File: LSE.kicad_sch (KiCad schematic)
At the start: 4 parts, among them Y2 32.758kHz

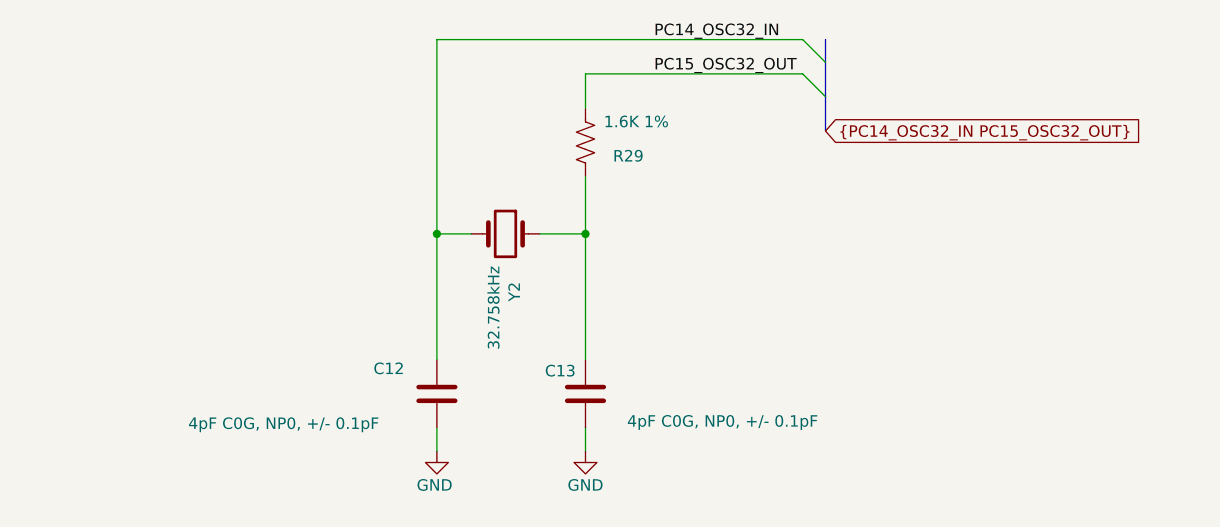
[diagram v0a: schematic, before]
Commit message: layout with F411 roughly good but needs work.
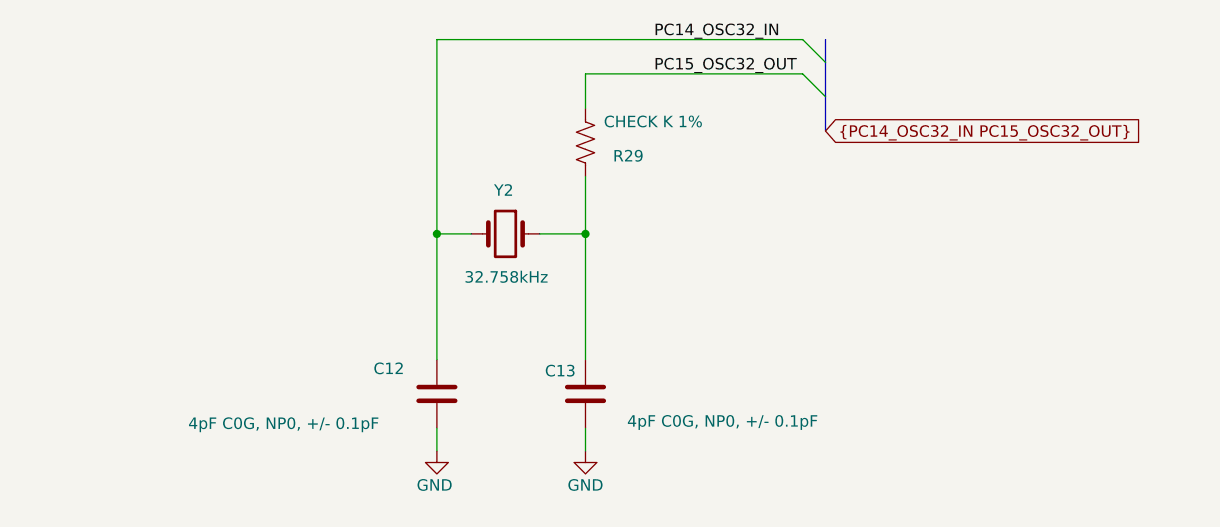
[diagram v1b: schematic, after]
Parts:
- C12, C13: footprint ProjectLib:C_0201_0603Metric -> ProjectLib:C_0603_1608Metric
- R29: value 1.6K 1% -> CHECK K 1%; footprint (none) -> ProjectLib:R_0603_1608Metric
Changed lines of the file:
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@@
 			)
 		)
-		(property "Footprint" "ProjectLib:C_0201_0603Metric"
+		(property "Footprint" "ProjectLib:C_0603_1608Metric"
 			(at 128.5748 109.22 0)
 			(effects
@@
 			)
 		)
-		(property "Footprint" "ProjectLib:C_0201_0603Metric"
+		(property "Footprint" "ProjectLib:C_0603_1608Metric"
 			(at 112.0648 109.22 0)
 			(effects
@@
 			)
 		)
-		(property "Value" "1.6K 1%"
+		(property "Value" "CHECK K 1%"
 			(at 131.572 82.804 0)
 			(effects
@@
 			)
 		)
-		(property "Footprint" ""
+		(property "Footprint" "ProjectLib:R_0603_1608Metric"
 			(at 130.556 85.344 90)
 			(effects
@@
 		(dnp no)
 		(property "Reference" "Y2"
-			(at 121.666 100.584 90)
+			(at 119.38 90.424 0)
 			(effects
 				(font
@@
 		)
 		(property "Value" "32.758kHz"
-			(at 119.38 98.806 90)
+			(at 116.078 100.076 0)
 			(effects
 				(font
@@
 			)
 		)
-		(property "Datasheet" "https://www.microcrystal.com/fileadmin/Media/Products/32kHz/Datasheet/CM9V-T1A.pdf"
+		(property "Datasheet" "~"
 			(at 120.65 95.25 0)
 			(effects

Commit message: Moats complete. No errors. Net tie needs better zone and check crystals, BoM, etc. And general review.
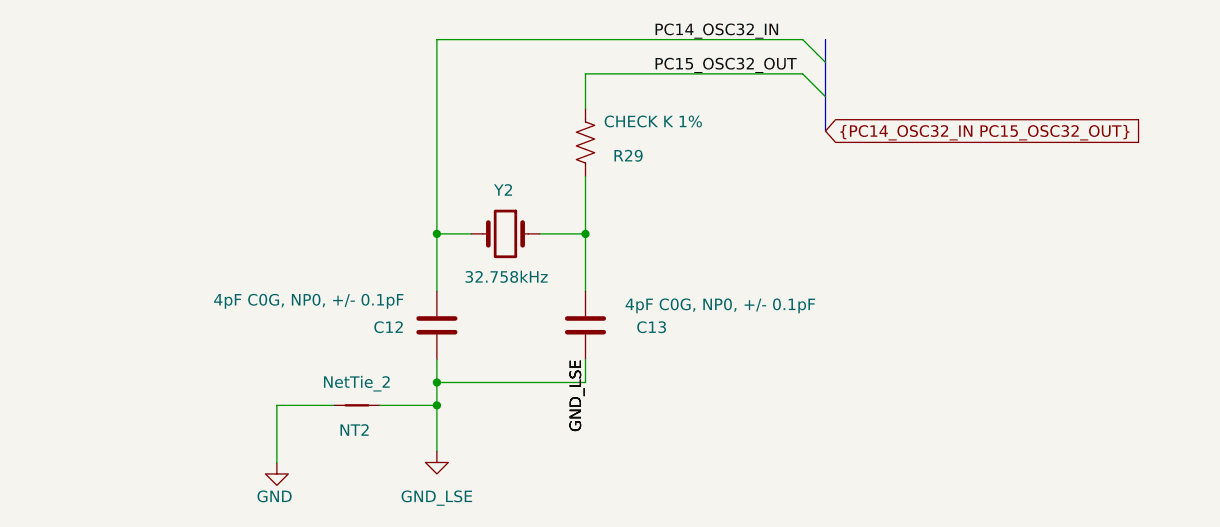
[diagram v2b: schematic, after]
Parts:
- added NT2: NetTie_2, ProjectLib:NetTie-2_SMD_Pad0.5mm, symbol ProjectLib:NetTie_2
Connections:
- net GND: now also NT2.1; no longer C12.1, C13.1
- new net GND_LSE: C12.1, C13.1, NT2.2
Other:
- moved on the sheet: C12, C13
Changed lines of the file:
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@@
+		(color 0 0 0 0)
+	)
+	(junction
+		(at 113.03 111.76)
+		(diameter 0)
+		(color 0 0 0 0)
+	)
+	(junction
+		(at 113.03 114.3)
+		(diameter 0)
 		(color 0 0 0 0)
 	)
@@
 	(wire
 		(pts
+			(xy 106.68 114.3) (xy 113.03 114.3)
+		)
+		(stroke
+			(width 0)
+			(type default)
+		)
+	)
+	(wire
+		(pts
 			(xy 129.54 95.25) (xy 124.46 95.25)
 		)
@@
 	(wire
 		(pts
+			(xy 113.03 111.76) (xy 113.03 114.3)
+		)
+		(stroke
+			(width 0)
+			(type default)
+		)
+	)
+	(wire
+		(pts
 			(xy 113.03 73.66) (xy 153.67 73.66)
 		)
@@
 	(wire
 		(pts
-			(xy 113.03 116.84) (xy 113.03 119.38)
+			(xy 101.6 114.3) (xy 95.25 114.3)
+		)
+		(stroke
+			(width 0)
+			(type default)
+		)
+	)
+	(wire
+		(pts
+			(xy 113.03 109.22) (xy 113.03 111.76)
 		)
 		(stroke
@@
 	(wire
 		(pts
-			(xy 129.54 95.25) (xy 129.54 109.22)
-		)
-		(stroke
-			(width 0)
-			(type default)
-		)
-	)
-	(wire
-		(pts
-			(xy 113.03 109.22) (xy 113.03 95.25)
+			(xy 129.54 95.25) (xy 129.54 101.6)
+		)
+		(stroke
+			(width 0)
+			(type default)
+		)
+	)
+	(wire
+		(pts
+			(xy 113.03 101.6) (xy 113.03 95.25)
 		)
 		(stroke
@@
 	(wire
 		(pts
-			(xy 129.54 119.38) (xy 129.54 116.84)
+			(xy 113.03 111.76) (xy 129.54 111.76)
+		)
+		(stroke
+			(width 0)
+			(type default)
+		)
+	)
+	(wire
+		(pts
+			(xy 129.54 111.76) (xy 129.54 109.22)
 		)
 		(stroke
@@
 		(pts
 			(xy 129.54 77.47) (xy 129.54 81.28)
+		)
+		(stroke
+			(width 0)
+			(type default)
+		)
+	)
+	(wire
+		(pts
+			(xy 95.25 114.3) (xy 95.25 120.65)
+		)
+		(stroke
+			(width 0)
+			(type default)
+		)
+	)
+	(wire
+		(pts
+			(xy 113.03 114.3) (xy 113.03 119.38)
 		)
 		(stroke
@@
 			)
 			(justify left bottom)
+		)
+	)
+	(label "GND_LSE"
+		(at 129.54 109.22 270)
+		(effects
+			(font
+				(size 1.27 1.27)
+			)
+			(justify right bottom)
+		)
+	)
+	(label "GND_LSE"
+		(at 129.54 109.22 270)
+		(effects
+			(font
+				(size 1.27 1.27)
+			)
+			(justify right bottom)
 		)
 	)
@@
 	(symbol
 		(lib_id "ProjectLib:C")
-		(at 129.54 113.03 180)
+		(at 129.54 105.41 180)
 		(unit 1)
 		(exclude_from_sim no)
@@
 		(dnp no)
 		(property "Reference" "C13"
-			(at 126.746 110.49 0)
+			(at 136.906 105.664 0)
 			(effects
 				(font
@@
 		)
 		(property "Value" "4pF C0G, NP0, +/- 0.1pF"
-			(at 144.78 116.078 0)
+			(at 144.526 103.124 0)
 			(effects
 				(font
@@
 		)
 		(property "Footprint" "ProjectLib:C_0603_1608Metric"
-			(at 128.5748 109.22 0)
+			(at 128.5748 101.6 0)
 			(effects
 				(font
@@
 		)
 		(property "Datasheet" "~"
-			(at 129.54 113.03 0)
+			(at 129.54 105.41 0)
 			(effects
 				(font
@@
 		)
 		(property "Description" "Unpolarized capacitor"
-			(at 129.54 113.03 0)
+			(at 129.54 105.41 0)
 			(effects
 				(font
@@
 		)
 		(property "MountType" "SMT"
-			(at 129.54 113.03 0)
+			(at 129.54 105.41 0)
 			(effects
 				(font
@@
 	(symbol
 		(lib_id "ProjectLib:C")
-		(at 113.03 113.03 180)
+		(at 113.03 105.41 180)
 		(unit 1)
 		(exclude_from_sim no)
@@
 		(dnp no)
 		(property "Reference" "C12"
-			(at 107.696 110.236 0)
+			(at 107.696 105.664 0)
 			(effects
 				(font
@@
 		)
 		(property "Value" "4pF C0G, NP0, +/- 0.1pF"
-			(at 96.012 116.332 0)
+			(at 98.806 102.616 0)
 			(effects
 				(font
@@
 		)
 		(property "Footprint" "ProjectLib:C_0603_1608Metric"
-			(at 112.0648 109.22 0)
+			(at 112.0648 101.6 0)
 			(effects
 				(font
@@
 		)
 		(property "Datasheet" "~"
-			(at 113.03 113.03 0)
+			(at 113.03 105.41 0)
 			(effects
 				(font
@@
 		)
 		(property "Description" "Unpolarized capacitor"
-			(at 113.03 113.03 0)
+			(at 113.03 105.41 0)
 			(effects
 				(font
@@
 		)
 		(property "MountType" "SMT"
-			(at 113.03 113.03 0)
+			(at 113.03 105.41 0)
 			(effects
 				(font
@@
 	)
 	(symbol
-		(lib_id "power:GND")
-		(at 129.54 119.38 0)
+		(lib_id "ProjectLib:NetTie_2")
+		(at 104.14 114.3 0)
 		(unit 1)
 		(exclude_from_sim no)
-		(in_bom yes)
+		(in_bom no)
 		(on_board yes)
 		(dnp no)
-		(property "Reference" "#PWR094"
-			(at 129.54 125.73 0)
-			(effects
-				(font
-					(size 1.27 1.27)
-				)
-				(hide yes)
-			)
-		)
-		(property "Value" "GND"
-			(at 129.54 123.19 0)
-			(effects
-				(font
-					(size 1.27 1.27)
-				)
-			)
-		)
-		(property "Footprint" ""
-			(at 129.54 119.38 0)
-			(effects
-				(font
-					(size 1.27 1.27)
-				)
-				(hide yes)
-			)
-		)
-		(property "Datasheet" ""
-			(at 129.54 119.38 0)
-			(effects
-				(font
-					(size 1.27 1.27)
-				)
-				(hide yes)
-			)
-		)
-		(property "Description" "Power symbol creates a global label with name \"GND\" , ground"
-			(at 129.54 119.38 0)
-			(effects
-				(font
-					(size 1.27 1.27)
-				)
-				(hide yes)
-			)
+		(property "Reference" "NT2"
+			(at 103.886 117.094 0)
+			(effects
+				(font
+					(size 1.27 1.27)
+				)
+			)
+		)
+		(property "Value" "NetTie_2"
+			(at 104.14 111.76 0)
+			(effects
+				(font
+					(size 1.27 1.27)
+				)
+			)
+		)
+		(property "Footprint" "ProjectLib:NetTie-2_SMD_Pad0.5mm"
+			(at 104.14 114.3 0)
+			(effects
+				(font
+					(size 1.27 1.27)
+				)
+				(hide yes)
+			)
+		)
+		(property "Datasheet" "~"
+			(at 104.14 114.3 0)
+			(effects
+				(font
+					(size 1.27 1.27)
+				)
+				(hide yes)
+			)
+		)
+		(property "Description" "Net tie, 2 pins"
+			(at 104.14 114.3 0)
+			(effects
+				(font
+					(size 1.27 1.27)
+				)
+				(hide yes)
+			)
+		)
+		(pin "2"
 		)
 		(pin "1"
 		)
 		(instances
-			(project "SensorProject_t16-pcb"
+			(project ""
 				(path "/0c2d0c14-8850-4a30-bb78-b2f40cb442ba/f12d0b95-be3f-41e2-8b41-943aec5e1edf/349f89d2-b212-45c7-8a70-67b2942fde7b"
-					(reference "#PWR094")
+					(reference "NT2")
 					(unit 1)
 				)
@@
 	(symbol
 		(lib_id "power:GND")
-		(at 113.03 119.38 0)
+		(at 95.25 120.65 0)
 		(unit 1)
 		(exclude_from_sim no)
@@
 		(dnp no)
 		(property "Reference" "#PWR093"
-			(at 113.03 125.73 0)
+			(at 95.25 127 0)
 			(effects
 				(font
@@
 		)
 		(property "Value" "GND"
-			(at 112.776 123.19 0)
+			(at 94.996 124.46 0)
 			(effects
 				(font
@@
 		)
 		(property "Footprint" ""
-			(at 113.03 119.38 0)
+			(at 95.25 120.65 0)
 			(effects
 				(font
@@
 		)
 		(property "Datasheet" ""
-			(at 113.03 119.38 0)
+			(at 95.25 120.65 0)
 			(effects
 				(font
@@
 		)
 		(property "Description" "Power symbol creates a global label with name \"GND\" , ground"
-			(at 113.03 119.38 0)
+			(at 95.25 120.65 0)
 			(effects
 				(font
@@
 					(unit 1)
 				)
+			)
+		)
+	)
+	(symbol
+		(lib_id "ProjectLib:GND_LSE")
+		(at 113.03 119.38 0)
+		(unit 1)
+		(exclude_from_sim no)
+		(in_bom yes)
+		(on_board yes)
+		(dnp no)
+		(fields_autoplaced yes)
+		(property "Reference" "#PWR062"
+			(at 113.03 125.73 0)
+			(effects
+				(font
+					(size 1.27 1.27)
+				)
+				(hide yes)
+			)
+		)
+		(property "Value" "GND_LSE"
+			(at 113.03 124.46 0)
+			(effects
+				(font
+					(size 1.27 1.27)
+				)
+			)
+		)
+		(property "Footprint" ""
+			(at 113.03 119.38 0)
+			(effects
+				(font
+					(size 1.27 1.27)
+				)
+				(hide yes)
+			)
+		)
+		(property "Datasheet" ""
+			(at 113.03 119.38 0)
+			(effects
+				(font
+					(size 1.27 1.27)
+				)
+				(hide yes)
+			)
+		)
+		(property "Description" "Power symbol creates a global label with name \"GND\" , ground"
+			(at 113.03 119.38 0)
+			(effects
+				(font
+					(size 1.27 1.27)
+				)
+				(hide yes)
+			)
+		)
+		(pin "1"
+		)
+		(instances
+			(project ""
+				(path "/0c2d0c14-8850-4a30-bb78-b2f40cb442ba/f12d0b95-be3f-41e2-8b41-943aec5e1edf/349f89d2-b212-45c7-8a70-67b2942fde7b"
+					(reference "#PWR062")
+					(unit 1)
+				)

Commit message: near complete, DRC good, ERC has a spurious error about ground on Y1.
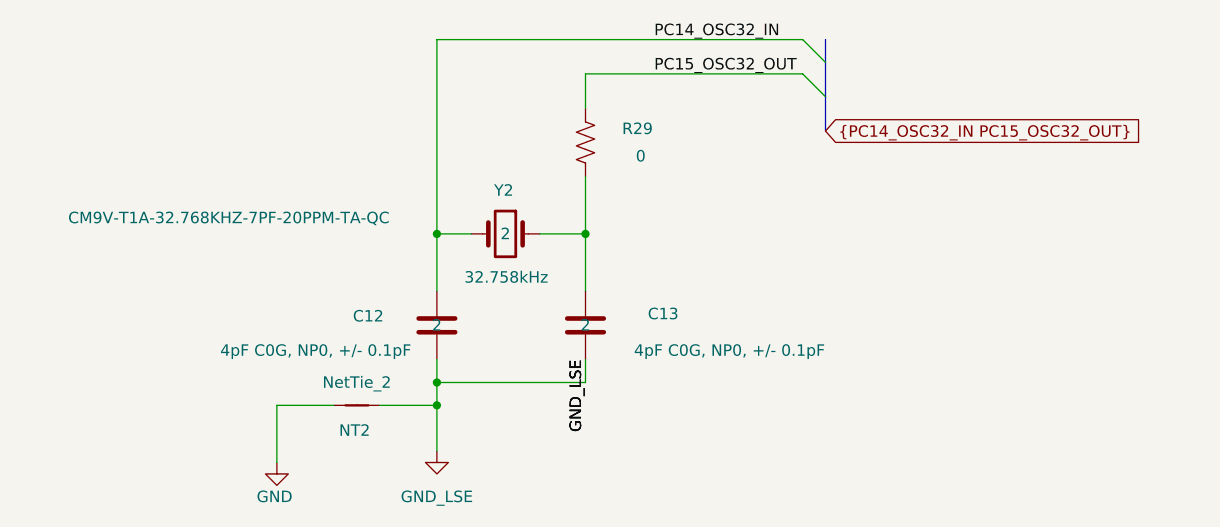
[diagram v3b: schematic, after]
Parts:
- C12, C13, Y2: pads (none) -> 2
- R29: value CHECK K 1% -> 0; MountType (none) -> SMT; pads (none) -> 2
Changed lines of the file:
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@@
 		(dnp no)
 		(property "Reference" "C13"
-			(at 136.906 105.664 0)
+			(at 138.176 104.14 0)
 			(effects
 				(font
@@
 		)
 		(property "Value" "4pF C0G, NP0, +/- 0.1pF"
-			(at 144.526 103.124 0)
+			(at 145.542 108.204 0)
 			(effects
 				(font
@@
 				)
 				(hide yes)
+			)
+		)
+		(property "pads" "2"
+			(at 129.54 105.41 0)
+			(effects
+				(font
+					(size 1.27 1.27)
+				)
 			)
 		)
@@
 		(dnp no)
 		(property "Reference" "C12"
-			(at 107.696 105.664 0)
+			(at 105.41 104.394 0)
 			(effects
 				(font
@@
 		)
 		(property "Value" "4pF C0G, NP0, +/- 0.1pF"
-			(at 98.806 102.616 0)
+			(at 99.568 108.204 0)
 			(effects
 				(font
@@
 				)
 				(hide yes)
+			)
+		)
+		(property "pads" "2"
+			(at 113.03 105.41 0)
+			(effects
+				(font
+					(size 1.27 1.27)
+				)
 			)
 		)
@@
 			)
 		)
+		(property "pads" ""
+			(at 104.14 114.3 0)
+			(effects
+				(font
+					(size 1.27 1.27)
+				)
+			)
+		)
 		(pin "2"
 		)
@@
 		(dnp no)
 		(property "Reference" "R29"
-			(at 132.588 86.614 0)
+			(at 133.604 83.566 0)
 			(effects
 				(font
@@
 			)
 		)
-		(property "Value" "CHECK K 1%"
-			(at 131.572 82.804 0)
+		(property "Value" "0"
+			(at 135.128 86.614 0)
 			(effects
 				(font
@@
 		)
 		(property "Description" "Resistor, US symbol"
+			(at 129.54 85.09 0)
+			(effects
+				(font
+					(size 1.27 1.27)
+				)
+				(hide yes)
+			)
+		)
+		(property "MountType" "SMT"
+			(at 129.54 85.09 0)
+			(effects
+				(font
+					(size 1.27 1.27)
+				)
+				(hide yes)
+			)
+		)
+		(property "pads" "2"
 			(at 129.54 85.09 0)
 			(effects
@@
 			)
 		)
-		(property "Datasheet" "~"
-			(at 120.65 95.25 0)
-			(effects
-				(font
-					(size 1.27 1.27)
-				)
-				(hide yes)
-			)
-		)
-		(property "Description" "Two pin crystal"
+		(property "Datasheet" "https://www.microcrystal.com/fileadmin/Media/Products/32kHz/Datasheet/CM9V-T1A.pdf"
+			(at 120.65 95.25 0)
+			(effects
+				(font
+					(size 1.27 1.27)
+				)
+				(hide yes)
+			)
+		)
+		(property "Description" "Two pin crystal, 7pF"
 			(at 120.65 95.25 0)
 			(effects
@@
 		)
 		(property "MfgPart" "CM9V-T1A-32.768KHZ-7PF-20PPM-TA-QC"
-			(at 120.65 95.25 0)
-			(effects
-				(font
-					(size 1.27 1.27)
-				)
-				(hide yes)
-			)
-		)
+			(at 89.916 93.472 0)
+			(effects
+				(font
+					(size 1.27 1.27)
+				)
+			)
+		)
+		(property "pads" "2"
+			(at 120.65 95.25 0)
+			(effects
+				(font
+					(size 1.27 1.27)
+				)
+			)
+		)

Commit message: cleanup, ready to submit.
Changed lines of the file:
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@@
 		(dnp no)
 		(property "Reference" "C13"
-			(at 138.176 104.14 0)
+			(at 135.89 104.394 0)
 			(effects
 				(font
@@
 		)
 		(property "Value" "4pF C0G, NP0, +/- 0.1pF"
-			(at 145.542 108.204 0)
+			(at 147.066 106.934 0)
 			(effects
 				(font
@@
 					(size 1.27 1.27)
 				)
+				(hide yes)
 			)
 		)
@@
 		)
 		(property "Value" "4pF C0G, NP0, +/- 0.1pF"
-			(at 99.568 108.204 0)
+			(at 96.266 106.934 0)
 			(effects
 				(font
@@
 					(size 1.27 1.27)
 				)
+				(hide yes)
 			)
 		)
@@
 					(size 1.27 1.27)
 				)
-			)
-		)
+				(hide yes)
+			)
+		)

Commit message: As made,  t16-F411 v0.2.0 2025-05, with added notes about needed fixes and results from some testing.
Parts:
- C12, C13: Manufacturer (none) -> TDK Corp; MfgPart (none) -> CGA3E2C0G1H040CT0Y0N
- R29: Manufacturer (none) -> Yageo; MfgPart (none) -> RC0603FR-070RL
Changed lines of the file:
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@@
 			)
 		)
-		(property "Datasheet" "~"
+		(property "Datasheet" ""
 			(at 129.54 105.41 0)
 			(effects
@@
 		)
 		(property "pads" "2"
+			(at 129.54 105.41 0)
+			(effects
+				(font
+					(size 1.27 1.27)
+				)
+				(hide yes)
+			)
+		)
+		(property "Manufacturer" "TDK Corp"
+			(at 129.54 105.41 0)
+			(effects
+				(font
+					(size 1.27 1.27)
+				)
+				(hide yes)
+			)
+		)
+		(property "MfgPart" "CGA3E2C0G1H040CT0Y0N"
 			(at 129.54 105.41 0)
 			(effects
@@
 			)
 		)
-		(property "Datasheet" "~"
+		(property "Datasheet" ""
 			(at 113.03 105.41 0)
 			(effects
@@
 		)
 		(property "pads" "2"
+			(at 113.03 105.41 0)
+			(effects
+				(font
+					(size 1.27 1.27)
+				)
+				(hide yes)
+			)
+		)
+		(property "Manufacturer" "TDK Corp"
+			(at 113.03 105.41 0)
+			(effects
+				(font
+					(size 1.27 1.27)
+				)
+				(hide yes)
+			)
+		)
+		(property "MfgPart" "CGA3E2C0G1H040CT0Y0N"
 			(at 113.03 105.41 0)
 			(effects
@@
 			)
 		)
-		(property "Datasheet" "~"
+		(property "Datasheet" ""
 			(at 129.54 85.09 0)
 			(effects
@@
 			(at 129.54 85.09 0)
 			(effects
+				(font
+					(size 1.27 1.27)
+				)
+				(hide yes)
+			)
+		)
+		(property "Manufacturer" "Yageo"
+			(at 129.54 85.09 0)
+			(effects
+				(font
+					(size 1.27 1.27)
+				)
+				(hide yes)
+			)
+		)
+		(property "MfgPart" "RC0603FR-070RL"
+			(at 129.54 85.09 0)
+			(effects

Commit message: Added U.FL for antenna, with GND_ANT zone.
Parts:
- R29: symbol Device:R_US -> ProjectLib:R_US
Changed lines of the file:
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@@
 			)
 		)
-		(property "Datasheet" ""
+		(property "Datasheet" "~"
 			(at 129.54 105.41 0)
 			(effects
@@
 			)
 		)
-		(property "Datasheet" ""
+		(property "Datasheet" "~"
 			(at 113.03 105.41 0)
 			(effects
@@
 	)
 	(symbol
-		(lib_id "Device:R_US")
+		(lib_id "ProjectLib:R_US")
 		(at 129.54 85.09 0)
 		(unit 1)
@@
 			)
 		)
-		(property "Datasheet" ""
+		(property "Datasheet" "~"
 			(at 129.54 85.09 0)
 			(effects
@@
 			)
 		)
-		(property "Datasheet" "https://www.microcrystal.com/fileadmin/Media/Products/32kHz/Datasheet/CM9V-T1A.pdf"
+		(property "Datasheet" "~"
 			(at 120.65 95.25 0)
 			(effects
@@
 			)
 		)
-		(property "Description" "Two pin crystal, 7pF"
+		(property "Description" "Two pin crystal"
 			(at 120.65 95.25 0)
 			(effects

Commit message: BOM cleaned up.
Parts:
- C12, C13: Notes (none) -> or equivalent; Package (none) -> C_0603_1608Metric
- R29: Notes (none) -> or equivalent; Package (none) -> R_0603_1608Metric
- Y2: Notes (none) -> or equivalent; Package (none) -> Crystal_SMD_MicroCrystal_CM9V-T1A-2Pin_1.6x1.0mm
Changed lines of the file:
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@@
 			)
 		)
-		(property "Datasheet" "~"
+		(property "Datasheet" ""
 			(at 129.54 105.41 0)
 			(effects
@@
 		)
 		(property "MfgPart" "CGA3E2C0G1H040CT0Y0N"
+			(at 129.54 105.41 0)
+			(effects
+				(font
+					(size 1.27 1.27)
+				)
+				(hide yes)
+			)
+		)
+		(property "Package" "C_0603_1608Metric"
+			(at 129.54 105.41 0)
+			(effects
+				(font
+					(size 1.27 1.27)
+				)
+				(hide yes)
+			)
+		)
+		(property "Notes" "or equivalent"
 			(at 129.54 105.41 0)
 			(effects
@@
 			)
 		)
-		(property "Datasheet" "~"
+		(property "Datasheet" ""
 			(at 113.03 105.41 0)
 			(effects
@@
 		)
 		(property "MfgPart" "CGA3E2C0G1H040CT0Y0N"
+			(at 113.03 105.41 0)
+			(effects
+				(font
+					(size 1.27 1.27)
+				)
+				(hide yes)
+			)
+		)
+		(property "Package" "C_0603_1608Metric"
+			(at 113.03 105.41 0)
+			(effects
+				(font
+					(size 1.27 1.27)
+				)
+				(hide yes)
+			)
+		)
+		(property "Notes" "or equivalent"
 			(at 113.03 105.41 0)
 			(effects
@@
 			)
 		)
+		(property "Package" ""
+			(at 104.14 114.3 0)
+			(effects
+				(font
+					(size 1.27 1.27)
+				)
+				(hide yes)
+			)
+		)
 		(pin "2"
 		)
@@
 			)
 		)
-		(property "Datasheet" "~"
+		(property "Datasheet" ""
 			(at 129.54 85.09 0)
 			(effects
@@
 		)
 		(property "MfgPart" "RC0603FR-070RL"
+			(at 129.54 85.09 0)
+			(effects
+				(font
+					(size 1.27 1.27)
+				)
+				(hide yes)
+			)
+		)
+		(property "Package" "R_0603_1608Metric"
+			(at 129.54 85.09 0)
+			(effects
+				(font
+					(size 1.27 1.27)
+				)
+				(hide yes)
+			)
+		)
+		(property "Notes" "or equivalent"
 			(at 129.54 85.09 0)
 			(effects
@@
 			)
 		)
-		(property "Datasheet" "~"
-			(at 120.65 95.25 0)
-			(effects
-				(font
-					(size 1.27 1.27)
-				)
-				(hide yes)
-			)
-		)
-		(property "Description" "Two pin crystal"
+		(property "Datasheet" "https://www.microcrystal.com/fileadmin/Media/Products/32kHz/Datasheet/CM9V-T1A.pdf"
+			(at 120.65 95.25 0)
+			(effects
+				(font
+					(size 1.27 1.27)
+				)
+				(hide yes)
+			)
+		)
+		(property "Description" "Two pin crystal, 7pF"
 			(at 120.65 95.25 0)
 			(effects
@@
 			)
 		)
-		(property "Notes" ""
+		(property "Notes" "or equivalent"
 			(at 120.65 95.25 0)
 			(effects
@@
 			(at 120.65 95.25 0)
 			(effects
+				(font
+					(size 1.27 1.27)
+				)
+				(hide yes)
+			)
+		)
+		(property "Package" "Crystal_SMD_MicroCrystal_CM9V-T1A-2Pin_1.6x1.0mm"
+			(at 120.65 95.25 0)
+			(effects
